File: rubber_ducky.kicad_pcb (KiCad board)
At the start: 2 copper layers, 3 parts, among them U1 ATmega32U4-A

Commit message: first demo
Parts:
- added C2: 20pF, Capacitor_SMD:C_0805_2012Metric_Pad1.18x1.45mm_HandSolder, F.Cu at (166.2, 99.6)
- added C4: 20pF, Capacitor_SMD:C_0805_2012Metric_Pad1.18x1.45mm_HandSolder, F.Cu at (171.4, 92.6)
- added R1: 22Ω, Resistor_SMD:R_0805_2012Metric_Pad1.20x1.40mm_HandSolder, F.Cu at (145.0, 89.8)
- added R2: 22Ω, Resistor_SMD:R_0805_2012Metric_Pad1.20x1.40mm_HandSolder, F.Cu at (145.0, 87.8)
- added U2: USB-C-2.0, usb-c-2.0:usb-c-2.0-MODULE, F.Cu at (135.2, 89.7)
- added Y1: ASCO, SMD3225:Crystal_SMD_3225-4Pin_3.2x2.5mm_HandSoldering, F.Cu at (166.4, 94.8)
- moved C1 4.36 mm to (142.4, 93.8), turned to 180 degrees
- moved C3 2.15 mm to (146.4, 95.0), turned to 90 degrees
- renumbered C2 to C3
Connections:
- net VBUS renamed +5V
- U1 pad 16: unconnected-(U1-XTAL2-Pad16) -> Net-(U1-XTAL2)
- U1 pad 17: unconnected-(U1-XTAL1-Pad17) -> Net-(U1-XTAL1)
- U1 pad 3: unconnected-(U1-D--Pad3) -> Net-(U1-D-)
- U1 pad 4: unconnected-(U1-D+-Pad4) -> Net-(U1-D+)
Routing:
- net +5V: track 0.00 -> 41.7 mm
- net Net-(U1-XTAL1): track 0.00 -> 23.2 mm
- net Net-(U1-XTAL2): track 0.00 -> 15.8 mm
- net Net-(U2-D+): track 0.00 -> 10.8 mm
- net Net-(U2-D-): track 0.00 -> 10.6 mm
- net Net-(U1-UCAP): track 0.00 -> 8.31 mm
- net GND: track 5.60 -> 0.00 mm
- net Net-(U1-D+): track 0.00 -> 3.92 mm
- net Net-(U1-D-): track 0.00 -> 3.89 mm
- net Net-(U1-VBUS): track 7.62 -> 4.85 mm
- added copper zone on F.Cu, net GND

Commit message: hotfix v0.1
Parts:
- moved Y1 3.81 mm to (166.6, 91.0)
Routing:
- net +5V: track 41.7 -> 0.00 mm
- net Net-(U1-XTAL1): track 23.2 -> 0.00 mm
- net Net-(U1-XTAL2): track 15.8 -> 0.00 mm
- net Net-(U2-D+): track 10.8 -> 0.00 mm
- net Net-(U2-D-): track 10.6 -> 0.00 mm
- net Net-(U1-UCAP): track 8.31 -> 0.00 mm
- net Net-(U1-VBUS): track 4.85 -> 0.00 mm
- net Net-(U1-D+): track 3.92 -> 0.00 mm
- net Net-(U1-D-): track 3.89 -> 0.00 mm
- removed copper zone on F.Cu, net GND

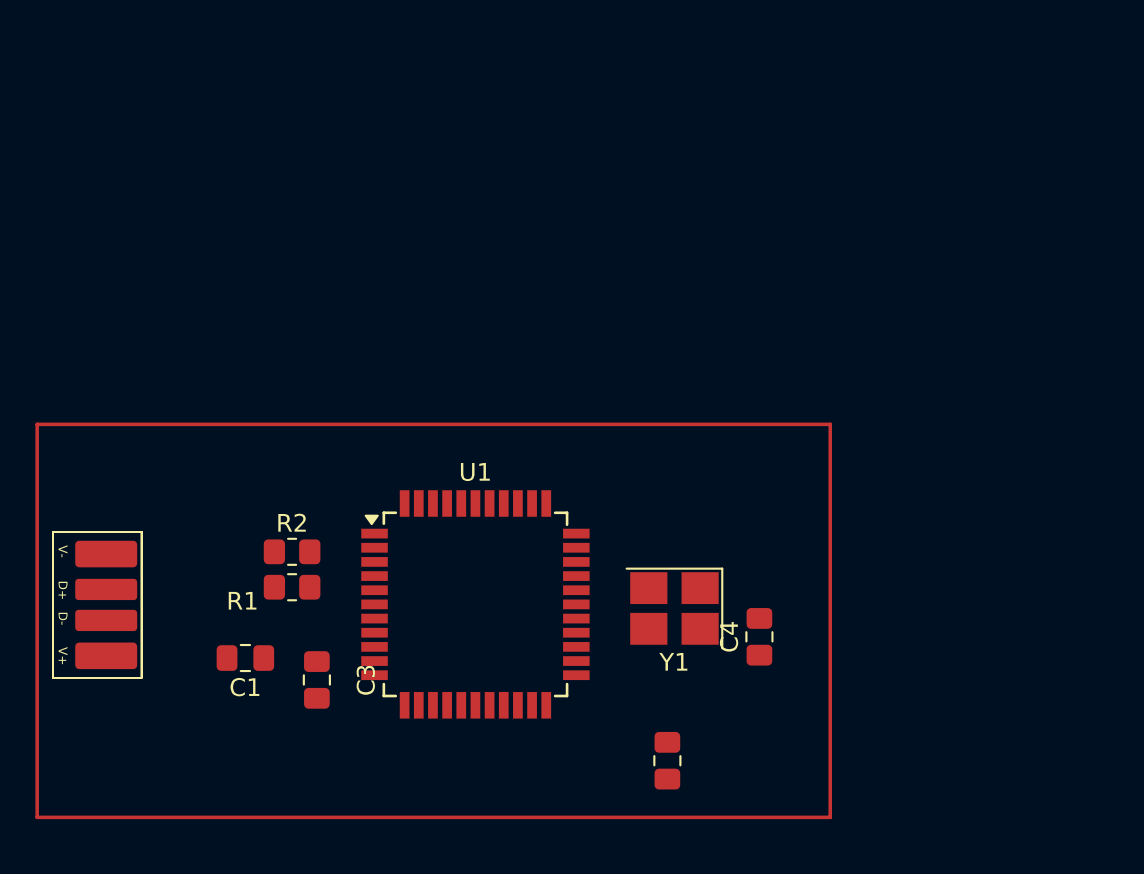
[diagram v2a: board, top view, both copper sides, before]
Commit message: rotation of atmega
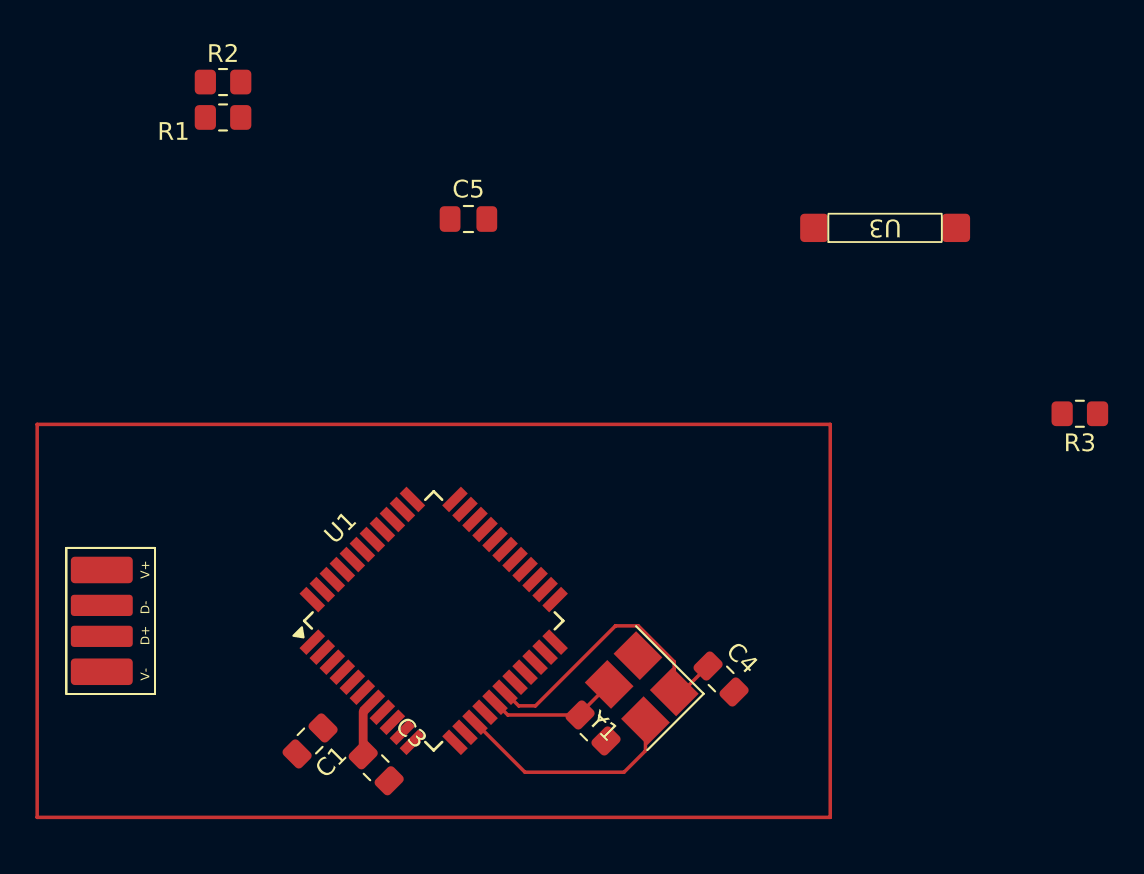
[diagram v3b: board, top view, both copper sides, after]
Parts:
- added C5: 100n, Capacitor_SMD:C_0805_2012Metric_Pad1.18x1.45mm_HandSolder, F.Cu at (155.0, 69.0)
- added R3: 10k, Resistor_SMD:R_0805_2012Metric_Pad1.20x1.40mm_HandSolder, F.Cu at (189.5, 80.0)
- added U3: ~, usb-c-2.0:switch, F.Cu at (178.5, 69.5)
- C1: value 1μF -> 1u
- C2, C4: value 20pF -> 20p
- C3: value 10μF -> 10u
- R1, R2: value 22Ω -> 22
- moved R1 26.8 mm to (141.1, 63.3)
- moved R2 26.8 mm to (141.1, 61.3)
- moved C3 5.99 mm to (149.8, 100.0), turned to 135 degrees
- moved C1 5.94 mm to (146.0, 98.5), turned to -135 degrees
- moved Y1 4.87 mm to (164.8, 95.5), turned to 135 degrees
- moved C2 4.59 mm to (162.0, 97.8), turned to -45 degrees
- moved U2 3.60 mm to (133.5, 92.8), turned to 90 degrees
- moved C4 3.22 mm to (169.2, 95.0), turned to -45 degrees
- moved U1 2.53 mm to (153.0, 91.7), turned to 45 degrees
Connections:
- C3 pad 1: GND -> +5V
- U1 pad 13: unconnected-(U1-~{RESET}-Pad13) -> Net-(U1-~{RESET})
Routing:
- net Net-(U1-XTAL1): track 0.00 -> 17.0 mm
- net +5V: track 0.00 -> 13.0 mm
- net Net-(U1-XTAL2): track 0.00 -> 7.51 mm
- net Net-(U1-VBUS): track 0.00 -> 3.19 mm

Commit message: hotfix v0.3
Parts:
- added D1: LED, LED_SMD:LED_0805_2012Metric_Pad1.15x1.40mm_HandSolder, F.Cu at (160.3, 85.2)
- added R4: 220, Resistor_SMD:R_0805_2012Metric_Pad1.20x1.40mm_HandSolder, F.Cu at (163.5, 88.3)
- added REF**: R_0805_2012Metric_Pad1.20x1.40mm_HandSolder, Resistor_SMD:R_0805_2012Metric_Pad1.20x1.40mm_HandSolder, F.Cu at (157.5, 99.7)
- moved R2 33.8 mm to (141.1, 95.1), turned to 135 degrees
- moved C5 32.9 mm to (148.4, 101.2), turned to 135 degrees
- moved R1 32.7 mm to (145.5, 95.7), turned to 135 degrees
- moved R3 29.2 mm to (168.2, 100.0), turned to 0 degrees
- moved U3 28.0 mm to (173.4, 97.0), turned to 180 degrees
- moved C2 1.78 mm to (160.2, 98.0)
- moved C1 0.50 mm to (146.3, 98.9)
- moved Y1 0.46 mm to (164.3, 95.7)
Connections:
- U1 pad 29: unconnected-(U1-PB5-Pad29) -> Net-(D1-A)
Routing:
- net Net-(U1-~{RESET}): track 0.00 -> 24.8 mm
- net +5V: track 13.0 -> 36.3 mm
- net GND: track 0.00 -> 13.9 mm
- net Net-(U2-D+): track 0.00 -> 12.1 mm
- net Net-(U2-D-): track 0.00 -> 6.89 mm
- net Net-(U1-D-): track 0.00 -> 6.56 mm
- net unconnected-(U1-PB0-Pad8): track 0.00 -> 5.36 mm, vias 0 -> 1
- net unconnected-(U1-PB1-Pad9): track 0.00 -> 4.37 mm, vias 0 -> 1
- net Net-(D1-A): track 0.00 -> 4.17 mm
- net unconnected-(U1-PB2-Pad10): track 0.00 -> 3.73 mm, vias 0 -> 1
- net Net-(U1-UCAP): track 0.00 -> 3.19 mm
- net Net-(U1-VBUS): track 3.19 -> 6.32 mm
- net unconnected-(U1-PB3-Pad11): track 0.00 -> 2.60 mm, vias 0 -> 1
- net Net-(U1-D+): track 0.00 -> 2.58 mm
- net Net-(D1-K): track 0.00 -> 2.47 mm
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- added copper zone on F.Cu, net GND

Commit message: v2
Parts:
- removed REF**: R_0805_2012Metric_Pad1.20x1.40mm_HandSolder, Resistor_SMD:R_0805_2012Metric_Pad1.20x1.40mm_HandSolder
- Y1: footprint SMD3225:Crystal_SMD_3225-4Pin_3.2x2.5mm_HandSoldering -> Crystal:Crystal_SMD_3225-4Pin_3.2x2.5mm_HandSoldering
- moved R4 21.4 mm to (144.6, 78.2), turned to -90 degrees
- moved U3 21.3 mm to (164.6, 77.6), turned to -90 degrees
- moved R3 20.0 mm to (165.6, 80.2), turned to 180 degrees
- moved D1 13.9 mm to (148.2, 78.2), turned to 90 degrees
- moved R2 10.6 mm to (142.2, 84.6), turned to 180 degrees
- moved C4 10.0 mm to (167.6, 85.1), turned to 45 degrees
- moved U2 9.49 mm to (137.3, 84.2), turned to -90 degrees
- moved C5 9.46 mm to (151.6, 92.3)
- moved R1 9.27 mm to (142.2, 87.0), turned to 180 degrees
- moved C1 8.84 mm to (148.1, 90.2), turned to 180 degrees
- moved C3 7.45 mm to (147.8, 92.8), turned to 0 degrees
- moved U1 6.96 mm to (155.5, 85.2)
- moved Y1 6.20 mm to (164.9, 89.5), turned to -135 degrees
- moved C2 5.73 mm to (159.9, 92.3), turned to -135 degrees
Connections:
- net Net-(U1-D+) renamed /D1+
- net Net-(U1-D-) renamed /D1-
- net Net-(U2-D+) renamed /D+
- net Net-(U2-D-) renamed /D-
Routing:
- net +5V: track 36.3 -> 84.6 mm, vias 0 -> 6
- net Net-(U1-XTAL1): track 17.0 -> 9.33 mm
- net /D+: track 12.1 -> 5.01 mm
- net Net-(D1-A): track 4.17 -> 11.1 mm, vias 0 -> 2
- net /D1+: track 2.58 -> 9.27 mm
- net unconnected-(U1-PB0-Pad8): track 5.36 -> 0.00 mm, vias 1 -> 0
- net unconnected-(U1-PB1-Pad9): track 4.37 -> 0.00 mm, vias 1 -> 0
- net Net-(U1-VBUS): track 6.32 -> 2.50 mm
- net unconnected-(U1-PB2-Pad10): track 3.73 -> 0.00 mm, vias 1 -> 0
- net Net-(U1-~{RESET}): track 24.8 -> 21.1 mm, vias 0 -> 2
- net unconnected-(U1-PB3-Pad11): track 2.60 -> 0.00 mm, vias 1 -> 0
- net /D1-: track 6.56 -> 8.89 mm
- net Net-(U1-XTAL2): track 5.73 -> 7.28 mm
- net /D-: track 6.89 -> 5.42 mm
- net Net-(D1-K): track 2.47 -> 3.62 mm
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
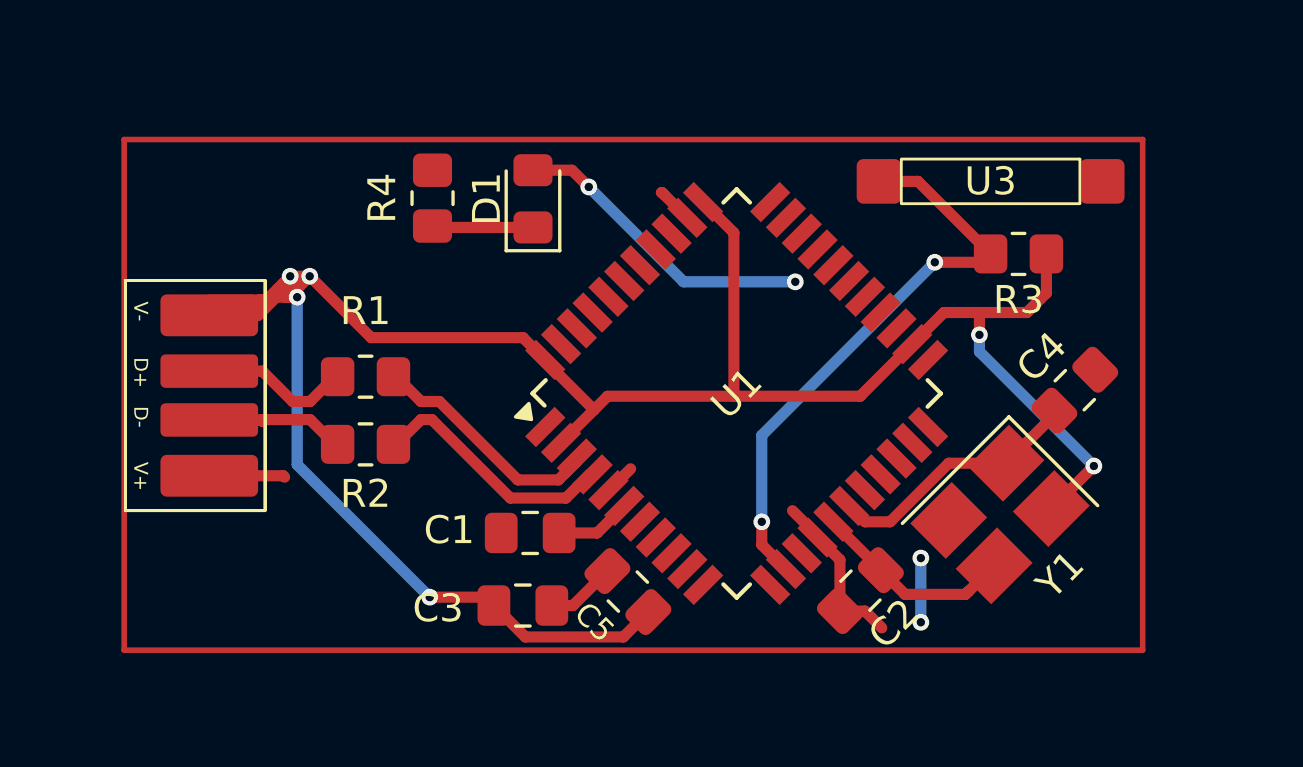
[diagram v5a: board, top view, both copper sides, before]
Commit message: correct USB c dimenstions
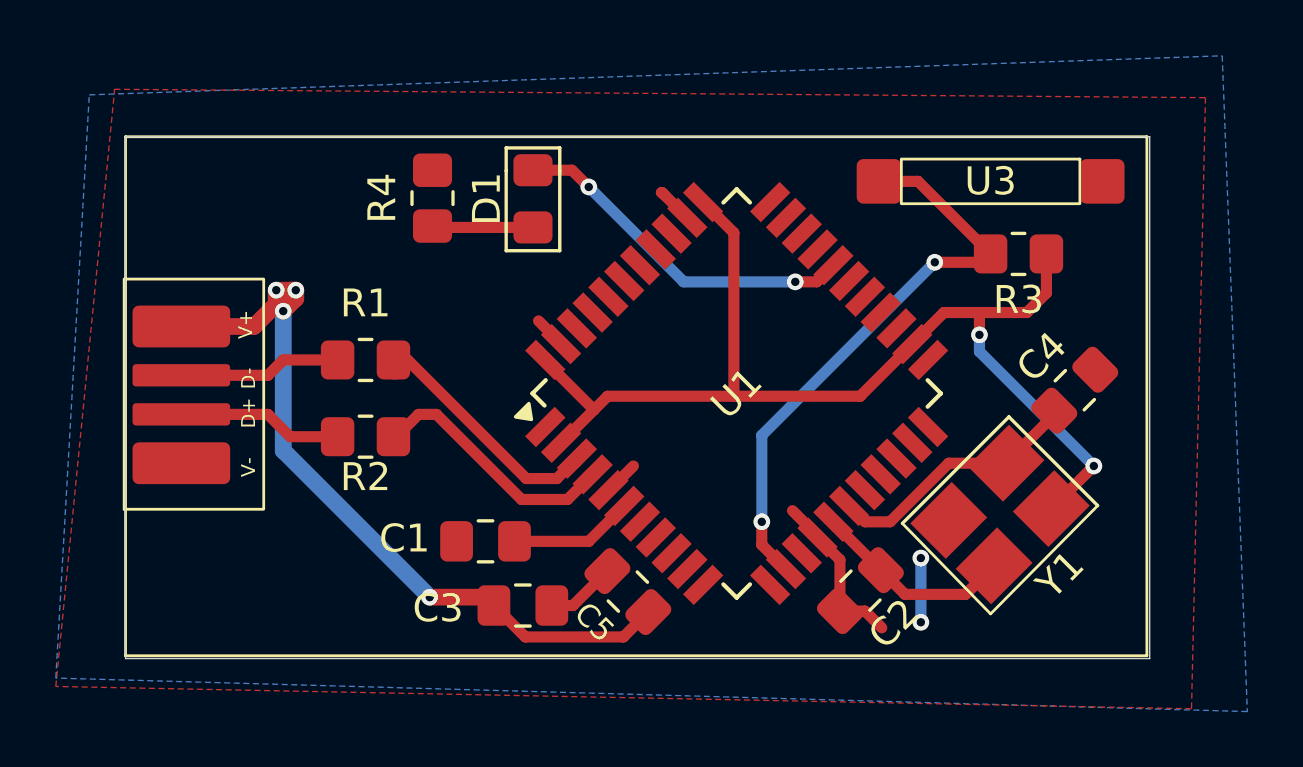
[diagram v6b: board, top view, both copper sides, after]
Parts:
- moved U2 2.07 mm to (135.6, 85.2), turned to 90 degrees
- moved C1 1.63 mm to (146.5, 90.5)
- moved R2 0.60 mm to (142.2, 84.0)
- moved R1 0.28 mm to (142.2, 86.8)
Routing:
- net +5V: track 84.6 -> 69.5 mm
- net Net-(U1-UCAP): track 2.73 -> 4.46 mm
- net Net-(D1-A): track 11.1 -> 12.7 mm
- net GND: track 13.6 -> 12.2 mm
- net /D+: track 5.01 -> 6.03 mm
- added copper zone on B.Cu, net GND
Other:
- board outline added: 36.7 x 18.7 mm
- board text added: "Aleksander Czarnecki 28.05.2025"
